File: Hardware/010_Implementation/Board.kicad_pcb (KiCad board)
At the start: 2 copper layers, 87.5 x 70 mm, 62 parts, among them IC1 SN65HVD233-HT, J1 Conn_01x08_Female, J2 JTAG Jumper Pins, J3 DSUB9, K1 G5V-2-DC5, K2 G5V-2-DC5, Q1 BC817, SW1 SW_Push, U1 TPS62160DGK, U2 ESP32-DEVKITC-32D

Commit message: Added Anchor points to PCB
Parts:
- added REF**: MountingHole_3.2mm_M3_DIN965_Pad, MountingHole:MountingHole_3.2mm_M3_DIN965_Pad, F.Cu at (47.5, 120.1)
- added REF**: MountingHole_3.2mm_M3_DIN965_Pad, MountingHole:MountingHole_3.2mm_M3_DIN965_Pad, F.Cu at (122.5, 120.1)
- added REF**: MountingHole_3.2mm_M3_DIN965_Pad, MountingHole:MountingHole_3.2mm_M3_DIN965_Pad, F.Cu at (47.5, 65.1)

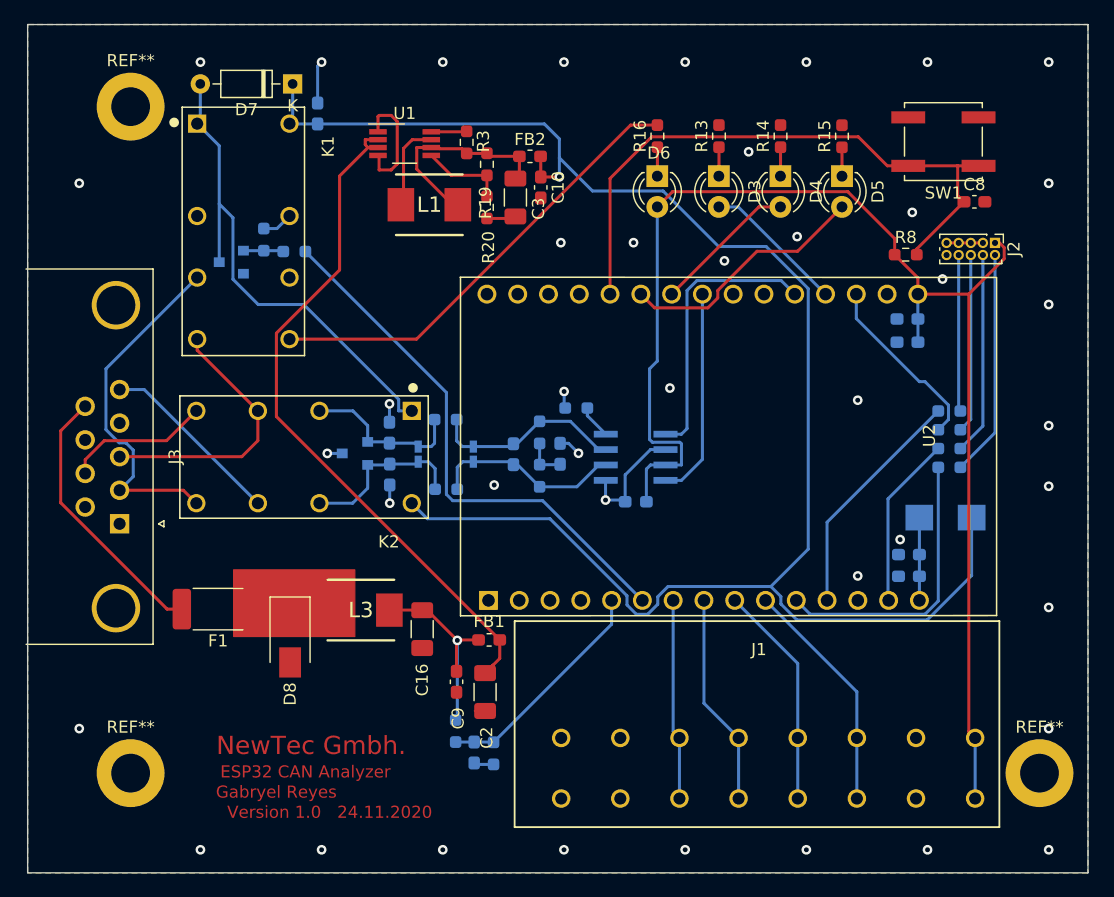
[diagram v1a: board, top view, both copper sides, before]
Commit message: Moved Pi-Filter to the top section. Added alignment marks on the back layer.
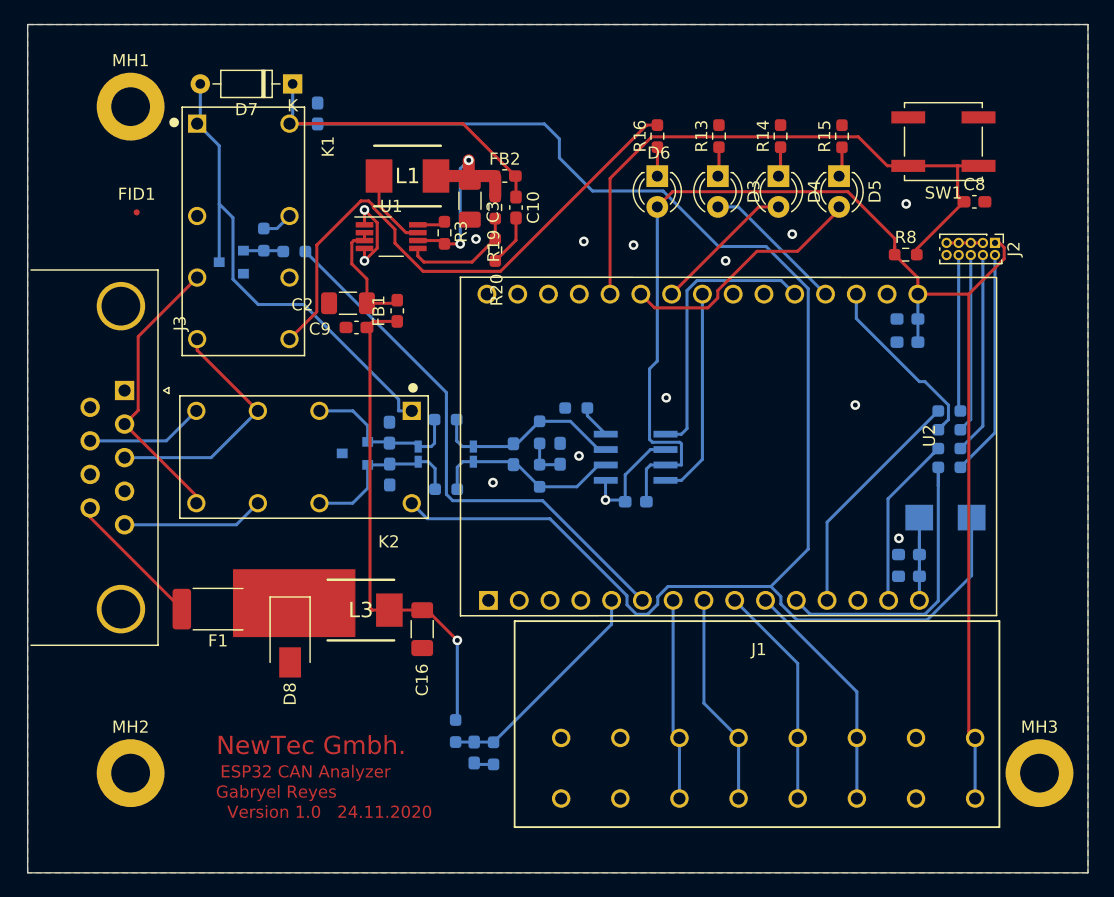
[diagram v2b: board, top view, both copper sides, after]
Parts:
- added FID1: Fiducial_0.5mm_Mask1mm, Fiducial:Fiducial_0.5mm_Mask1mm, F.Cu at (48.0, 73.8)
- J3: footprint Connector_Dsub:DSUB-9_Female_Horizontal_P2.77x2.84mm_EdgePinOffset4.94mm_Housed_MountingHolesOffset7.48mm -> Connector_Dsub:DSUB-9_Male_Horizontal_P2.77x2.84mm_EdgePinOffset4.94mm_Housed_MountingHolesOffset7.48mm
- moved C2 34.0 mm to (65.5, 81.3), turned to 180 degrees
- moved C9 30.4 mm to (66.2, 83.3), turned to 180 degrees
- moved FB1 28.2 mm to (69.5, 82.0), turned to 270 degrees
- moved J3 11.0 mm to (47.0, 88.5)
- moved U1 7.75 mm to (69.0, 75.8)
- moved R3 7.69 mm to (73.4, 75.5)
- moved C3 3.76 mm to (75.5, 72.9)
- moved R19 3.63 mm to (77.6, 73.5)
- moved R20 3.58 mm to (77.6, 77.0)
- moved L1 2.98 mm to (70.4, 70.8)
- moved FB2 2.64 mm to (78.4, 70.8)
- moved C10 2.63 mm to (79.3, 73.5)
- moved D5 0.24 mm to (106.0, 70.9)
- moved D4 0.16 mm to (101.0, 70.9)
- moved D3 0.08 mm to (96.0, 70.9)
- renumbered REF** to MH1, REF** to MH2, REF** to MH3
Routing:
- net Net-(C2-Pad1): track 58.1 -> 10.3 mm
- net Net-(C16-Pad1): track 18.1 -> 41.4 mm
- net +5V: track 143.0 -> 160.3 mm, vias 1 -> 0
- net GND: track 40.7 -> 28.6 mm, vias 42 -> 14
- net /Connector/OBD_VDD: track 22.4 -> 11.5 mm
- net /Connector/CAN_Mode: track 37.7 -> 46.5 mm
- net /Connector/Pin_2: track 29.2 -> 23.6 mm
- net Net-(C3-Pad1): track 17.2 -> 21.1 mm, vias 0 -> 2
- net /Connector/Pin_5: track 15.3 -> 11.7 mm
- net Net-(R19-Pad2): track 7.00 -> 9.69 mm
- net Net-(C12-Pad1): track 7.49 -> 9.72 mm
- net /Connector/Pin_7: track 12.2 -> 10.0 mm
- net /Connector/Pin_3: track 22.4 -> 20.6 mm
- net /MCU/MTMS: track 23.7 -> 25.2 mm
- net Net-(L1-Pad1): track 7.33 -> 6.57 mm
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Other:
- board text removed: "+5V"

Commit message: Board version 8 with gerber files
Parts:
- added C18: 100n, Capacitor_SMD:C_0603_1608Metric_Pad1.08x0.95mm_HandSolder, B.Cu at (73.5, 100.1)
- added D9: 1N4148, Diode_THT:D_DO-35_SOD27_P7.62mm_Horizontal, F.Cu at (63.1, 87.3)
- added MH4: MountingHole_3.2mm_M3_DIN965_Pad, MountingHole:MountingHole_3.2mm_M3_DIN965_Pad, F.Cu at (122.8, 121.8)
- C17: footprint Capacitor_SMD:C_0603_1608Metric_Pad1.05x0.95mm_HandSolder -> Capacitor_SMD:C_0603_1608Metric_Pad1.08x0.95mm_HandSolder
- moved MH1 56.6 mm to (47.8, 121.8)
- moved MH2 53.4 mm to (47.8, 66.8)
- moved MH3 53.4 mm to (122.8, 66.8)
- moved R8 24.4 mm to (87.1, 77.0), turned to 270 degrees
- moved R2 13.0 mm to (87.1, 109.7)
- moved C1 12.9 mm to (85.5, 109.7)
- moved R1 11.8 mm to (83.9, 109.7), turned to 90 degrees
- moved C9 8.08 mm to (65.8, 75.3), turned to 90 degrees
- moved C17 7.34 mm to (90.1, 90.4), turned to 0 degrees
- moved C2 7.16 mm to (67.8, 74.6), turned to 90 degrees
- moved D2 4.40 mm to (110.4, 99.2), turned to 180 degrees
- moved FB1 4.08 mm to (67.2, 78.6), turned to 180 degrees
- moved C8 4.00 mm to (113.2, 73.2), turned to 180 degrees
- moved C10 3.58 mm to (82.9, 73.4)
- moved FB2 3.58 mm to (82.0, 70.8)
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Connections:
- J1 pad 7: (no net) -> GND
- J1 pad 8: (no net) -> GND
- U2 pad 21: /MCU/Indicator_STA_Mode -> /MCU/Indicator_AP_Mode
- U2 pad 22: /MCU/Indicator_AP_Mode -> /MCU/Indicator_STA_Mode
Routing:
- net +5V: track 160.3 -> 118.6 mm, vias 0 -> 6
- net Net-(C16-Pad1): track 41.4 -> 56.9 mm, vias 1 -> 3
- net GND: track 28.6 -> 15.1 mm, vias 14 -> 423
- net /MCU/OBD_Voltage_Check: track 18.9 -> 6.27 mm
- net /Connector/~OBD~\CAN: track 44.7 -> 53.8 mm, vias 0 -> 2
- net Net-(L1-Pad1): track 6.57 -> 0.00 mm
- net Net-(D8-Pad1): track 7.35 -> 1.62 mm
- net Net-(C2-Pad1): track 10.3 -> 5.61 mm
- net /MCU/Indicator_STA_Mode: track 20.9 -> 16.8 mm
- net +3V3: track 113.4 -> 117.1 mm, vias 0 -> 6
- net /MCU/Indicator_AP_Mode: track 12.0 -> 14.3 mm
- net Net-(C3-Pad1): track 21.1 -> 23.0 mm
- net /MCU/WiFi_Mode: track 51.8 -> 50.3 mm, vias 0 -> 2
- net /Connector/CAN_Mode: track 46.5 -> 45.4 mm
- net Net-(C12-Pad1): track 9.72 -> 8.93 mm
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- added copper zone on F.Cu, net Net-(D8-Pad1)
- added copper zone on F.Cu, net Net-(L1-Pad1)
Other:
- board text removed: "+12V"
- board text removed: "Filter"

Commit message: Board Version 1.0 Review 3
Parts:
- moved U2 28.2 mm to (72.5, 107.5)
- moved C16 3.08 mm to (71.9, 111.3)
- moved D9 1.40 mm to (61.7, 87.3)
- moved C4 1.35 mm to (67.5, 92.0)
- moved C5 1.35 mm to (67.6, 95.5)
- moved D1 1.35 mm to (64.8, 93.7)
- moved K2 1.31 mm to (60.5, 94.0)
- moved J3 0.50 mm to (46.5, 88.5)
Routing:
- net GND: track 15.1 -> 24.6 mm, vias 423 -> 242
- net +5V: track 118.6 -> 123.9 mm, vias 6 -> 7
- net /Connector/CAN_Mode: track 45.4 -> 40.9 mm, vias 0 -> 2
- net /CAN_Transceiver/CAN_Tx: track 23.1 -> 19.9 mm
- net /MCU/Indicator_Error: track 11.8 -> 14.0 mm
- net /Connector/~OBD~\CAN: track 53.8 -> 52.3 mm
- net /Connector/Pin_3: track 20.6 -> 19.2 mm
- net /MCU/Indicator_STA_Mode: track 16.8 -> 15.4 mm
- net /CAN_Transceiver/CAN_Rx: track 17.4 -> 18.8 mm, vias 0 -> 1
- net /CAN_Transceiver/BUS_L: track 14.0 -> 15.3 mm
- net /MCU/Indicator_AP_Mode: track 14.3 -> 13.2 mm
- net Net-(C16-Pad1): track 56.9 -> 57.9 mm
- net /Connector/Pin_7: track 10.0 -> 8.97 mm
- net /CAN_Transceiver/BUS_H: track 13.6 -> 14.5 mm
- net Net-(C12-Pad1): track 8.93 -> 9.83 mm
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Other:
- board text added: "BOT"
- board text added: "NewTec GmbH."
- board text added: "TOP"
- board text added: "Version 1.0 27.11.2020"
- board text removed: "NewTec Gmbh."
- board text removed: "Version 1.0 24.11.2020"

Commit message: Board Version 1.0 Review 4
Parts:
- added FID2: Fiducial_0.5mm_Mask1mm, Fiducial:Fiducial_0.5mm_Mask1mm, B.Cu at (47.0, 73.8)
- J2: footprint Connector_PinHeader_1.00mm:PinHeader_2x05_P1.00mm_Vertical -> Connector_PinHeader_2.54mm:PinHeader_2x05_P2.54mm_Vertical
- moved C8 10.8 mm to (112.8, 62.5)
- moved J2 3.25 mm to (121.5, 74.4)
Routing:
- net GND: track 24.6 -> 32.2 mm, vias 242 -> 257
- net Net-(J2-Pad6): track 14.8 -> 20.4 mm
- net Net-(J2-Pad8): track 12.9 -> 17.2 mm
- net Net-(J2-Pad2): track 18.7 -> 21.8 mm
- net Net-(J2-Pad4): track 16.7 -> 19.7 mm
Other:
- board text added: "AP_Mode"
- board text added: "CAN BUS"
- board text added: "CAN_Mode"
- board text added: "ERROR"
- board text added: "ESP32- MODULE"
- board text added: "GND"
- board text added: "IO1"
- board text added: "IO2"
- board text added: "IO3"
- board text added: "IO4"
- board text added: "JTAG"
- board text added: "STA_Mode"
- board text added: "VCC"
- board text added: "WiFi_Mode"

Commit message: Board Version 1.0 Review 5
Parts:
- moved J2 0.12 mm to (121.4, 74.4)
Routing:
- net Net-(J2-Pad6): track 20.4 -> 17.4 mm
- net Net-(J2-Pad4): track 19.7 -> 18.7 mm
